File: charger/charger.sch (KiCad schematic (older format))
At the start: 1 part, among them U1 MSP432

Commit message: added aux power schem
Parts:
- added C1, C2: 1 uF, symbol Device:C_Small
- added C? (x2): 0.1 uF, symbol Device:C_Small
- added C?: 2.2 uF, symbol Device:CP
- added C?: 10 uF, symbol Device:CP
- added C?: 1 uF, symbol Device:CP
- added R?: 0 ohm, Resistor_SMD:R_1206_3216Metric, symbol Device:R_Small_US
- added R?: 0 ohm, symbol Device:R_Small_US
- added U2: NCP718xSN500, Package_TO_SOT_SMD:SOT-23-5, symbol Regulator_Linear:NCP718xSN500
- added U?: LF90_TO252, Package_TO_SOT_SMD:TO-252-2, symbol Regulator_Linear:LF90_TO252
- added U?: AP131-33, Package_TO_SOT_SMD:SOT-23-5, symbol Regulator_Linear:AP131-33
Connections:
- net labels added: +12V, +3.3V, +5V, +9V, GND
- wire segments 0 -> 60

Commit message: add power circuit
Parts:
- removed C?: 0.1 uF, symbol Device:C_Small
- removed C?: 2.2 uF, symbol Device:CP
- removed U?: LF90_TO252, Package_TO_SOT_SMD:TO-252-2, symbol Regulator_Linear:LF90_TO252
- added C?: 1000 uF, symbol Device:CP
- added C? (x3): 10 uF, symbol Device:C
- added C? (x2): 1000 pF, symbol Device:C
- added C? (x4): 1 uF, symbol Device:C
- added C?: 22 nF, symbol Device:C
- added C? (x2): 220 uF, symbol Device:C
- added C? (x2): 560 uF, symbol Device:C
- added C? (x2): 0.1 uF, symbol Device:C
- added D?: B1100B, symbol Device:D_Schottky
- added D? (x2): MUHA11013G, symbol Device:D
- added D? (x2): B1100-13, symbol Device:D_Schottky
- added L? (x2): 7443642200, symbol Device:L
- added L?: 220 uH, symbol Device:L
- added Q? (x4): CSD19531Q5A, Package_TO_SOT_SMD:TDSON-8-1, symbol Transistor_FET:CSD19531Q5A
- added R? (x2): 5.6 ohm, symbol Device:R_Small_US
- added R?: 430k, symbol Device:R_Small_US
- added R?: 169k, symbol Device:R_Small_US
- added R?: 3k, symbol Device:R_Small_US
- added R?: 3, symbol Device:R_Small_US
- added R?: 1k, symbol Device:R_Small_US
- added R? (x4): 2.21, symbol Device:R_Small_US
- added R? (x2): 4.42, symbol Device:R_Small_US
- added U?: LM5009MM, Package_SO:MSOP-8_3x3mm_P0.65mm, symbol Regulator_Switching:LM5009MM
- added U? (x2): LM5109BMA, Package_SO:SOIC-8_3.9x4.9mm_P1.27mm, symbol Driver_FET:LM5109BMA
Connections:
- net labels added: +10V, PWM_H1, PWM_H2, PWM_L1, PWM_L2, V_in, V_out, V_p
- net labels removed: +12V, +9V
- wire segments 60 -> 163

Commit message: added connectors
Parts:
- added J?: OSTT7020150, symbol Connector:Screw_Terminal_01x06
- added J?: OSTT7020150, symbol Connector:Screw_Terminal_01x02
- added TP? (x7): TestPoint, symbol Connector:TestPoint
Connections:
- net +10V: now also TP?.1
- net +3V3: now also TP?.1
- net +5V: now also TP?.1
- net at R?.2, U?.5 (LO): now also TP?.1 (x2)
- net at R?.2, U?.7 (HO): now also TP?.1 (x2)
- new net +BATT: J?.1 (Pin_1)
- new net -BATT: J?.2 (Pin_2)
- new net SP1+: J?.1 (Pin_1)
- new net SP1-: J?.2 (Pin_2), J?.3 (Pin_3)
- new net SP2-: J?.4 (Pin_4), J?.5 (Pin_5)
- new net SP3-: J?.6 (Pin_6)
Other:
- note added: "Based on TIDA-010042"
- note added: "Mark Ditsworth"
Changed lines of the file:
@@
 	9450 2550 9450 2650
 Wire Wire Line
-	10650 2250 10650 2550
+	10650 2250 10650 2400
 Connection ~ 10650 2550
 Wire Wire Line
@@
 Text Label 3650 3250 0    50   ~ 0
 PWM_L2
+$Comp
+L Connector:Screw_Terminal_01x06 J?
+U 1 1 5F1BBACF
+P 600 7350
+F 0 "J?" H 518 6917 50  0000 C CNN
+F 1 "OSTT7020150" H 680 7251 50  0001 L CNN
+F 2 "" H 600 7350 50  0001 C CNN
+F 3 "~" H 600 7350 50  0001 C CNN
+	1    600  7350
+	-1   0    0    1
+$EndComp
+$Comp
+L Connector:Screw_Terminal_01x02 J?
+U 1 1 5F1C245D
+P 6650 7400
+F 0 "J?" H 6730 7346 50  0000 L CNN
+F 1 "OSTT7020150" H 6730 7301 50  0001 L CNN
+F 2 "" H 6650 7400 50  0001 C CNN
+F 3 "~" H 6650 7400 50  0001 C CNN
+	1    6650 7400
+	1    0    0    -1
+$EndComp
+$Comp
+L Connector:TestPoint TP?
+U 1 1 5F1C5256
+P 9500 1050
+F 0 "TP?" V 9695 1122 50  0000 C CNN
+F 1 "TestPoint" V 9604 1122 50  0000 C CNN
+F 2 "" H 9700 1050 50  0001 C CNN
+F 3 "~" H 9700 1050 50  0001 C CNN
+	1    9500 1050
+	0    -1   -1   0
+$EndComp
+$Comp
+L Connector:TestPoint TP?
+U 1 1 5F1DAE48
+P 10750 1050
+F 0 "TP?" V 10704 1238 50  0000 L CNN
+F 1 "TestPoint" V 10795 1238 50  0000 L CNN
+F 2 "" H 10950 1050 50  0001 C CNN
+F 3 "~" H 10950 1050 50  0001 C CNN
+	1    10750 1050
+	0    1    1    0
+$EndComp
+$Comp
+L Connector:TestPoint TP?
+U 1 1 5F1DBECE
+P 10650 2400
+F 0 "TP?" V 10604 2588 50  0000 L CNN
+F 1 "TestPoint" V 10695 2588 50  0000 L CNN
+F 2 "" H 10850 2400 50  0001 C CNN
+F 3 "~" H 10850 2400 50  0001 C CNN
+	1    10650 2400
+	0    1    1    0
+$EndComp
+Connection ~ 10650 2400
+Wire Wire Line
+	10650 2400 10650 2550
+$Comp
+L Connector:TestPoint TP?
+U 1 1 5F1E3B56
+P 4950 2500
+F 0 "TP?" H 5008 2618 50  0000 L CNN
+F 1 "TestPoint" H 5008 2527 50  0000 L CNN
+F 2 "" H 5150 2500 50  0001 C CNN
+F 3 "~" H 5150 2500 50  0001 C CNN
+	1    4950 2500
+	1    0    0    -1
+$EndComp
+Connection ~ 4950 2500
+$Comp
+L Connector:TestPoint TP?
+U 1 1 5F1E6782
+P 5250 3350
+F 0 "TP?" V 5204 3538 50  0000 L CNN
+F 1 "TestPoint" V 5295 3538 50  0000 L CNN
+F 2 "" H 5450 3350 50  0001 C CNN
+F 3 "~" H 5450 3350 50  0001 C CNN
+	1    5250 3350
+	0    1    1    0
+$EndComp
+Connection ~ 5250 3350
+$Comp
+L Connector:TestPoint TP?
+U 1 1 5F1E781A
+P 5250 1750
+F 0 "TP?" V 5204 1938 50  0000 L CNN
+F 1 "TestPoint" V 5295 1938 50  0000 L CNN
+F 2 "" H 5450 1750 50  0001 C CNN
+F 3 "~" H 5450 1750 50  0001 C CNN
+	1    5250 1750
+	0    1    1    0
+$EndComp
+Connection ~ 5250 1750
+$Comp
+L Connector:TestPoint TP?
+U 1 1 5F1EFFDD
+P 4950 1000
+F 0 "TP?" H 5008 1118 50  0000 L CNN
+F 1 "TestPoint" H 5008 1027 50  0000 L CNN
+F 2 "" H 5150 1000 50  0001 C CNN
+F 3 "~" H 5150 1000 50  0001 C CNN
+	1    4950 1000
+	1    0    0    -1
+$EndComp
+Connection ~ 4950 1000
+Text Label 800  7550 0    50   ~ 0
+SP1+
+Text Label 800  7450 0    50   ~ 0
+SP1-
+Text Label 800  7350 0    50   ~ 0
+SP2+
+Text Label 800  7250 0    50   ~ 0
+SP2-
+Text Label 800  7150 0    50   ~ 0
+SP3+
+Text Label 800  7050 0    50   ~ 0
+SP3-
+Wire Wire Line
+	800  7350 800  7450
+Wire Wire Line
+	800  7150 800  7250
+$Comp
+L power:+BATT #PWR?
+U 1 1 5F24AB5C
+P 6450 7400
+F 0 "#PWR?" H 6450 7250 50  0001 C CNN
+F 1 "+BATT" H 6465 7573 50  0000 C CNN
+F 2 "" H 6450 7400 50  0001 C CNN
+F 3 "" H 6450 7400 50  0001 C CNN
+	1    6450 7400
+	1    0    0    -1
+$EndComp
+$Comp
+L power:-BATT #PWR?
+U 1 1 5F24D3B8
+P 6450 7500
+F 0 "#PWR?" H 6450 7350 50  0001 C CNN
+F 1 "-BATT" H 6465 7673 50  0000 C CNN
+F 2 "" H 6450 7500 50  0001 C CNN
+F 3 "" H 6450 7500 50  0001 C CNN
+	1    6450 7500
+	-1   0    0    1
+$EndComp
+Text Notes 10150 7350 0    89   ~ 0
+Mark Ditsworth
+Text Notes 7400 7500 0    89   ~ 0
+Based on TIDA-010042
 $EndSCHEMATC

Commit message: add ckt enable/disable
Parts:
- added C? (x2): 1200 uF, symbol Device:CP
- added C? (x5): 4.7 uF, symbol Device:C
- added C?: 0.1 uF, symbol Device:C
- added D?: D_Zener, symbol Device:D_Zener
- added Q? (x2): CSD18540Q5B, Package_TO_SOT_SMD:TDSON-8-1, symbol Transistor_FET:CSD18540Q5B
- added R? (x2): 0.002, symbol Device:R_US
- added R?: 5.11, symbol Device:R_US
- added R?: 10k, symbol Device:R_US
- added U?: UCC27517DBVR, symbol MSP_mwd:Generic_SOT23-5
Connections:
- net +10V: now also C?.2, U?.1
- net GND: now also C?.1, C?.2, C?.2, C?.2, C?.2, C?.2, C?.2, C?.2, D?.2 (A), Q?.1 (S), Q?.1 (S), Q?.2 (S), Q?.2 (S), Q?.3 (S), Q?.3 (S), U?.2, U?.4
- net SP1+: now also R?.2
- net SP3-: now also Q?.5 (D)
- net V_in: now also C?.1, C?.1, C?.1, C?.1, C?.1, C?.1, C?.1, R?.1
- net V_out: now also R?.1, R?.2
- net +BATT renamed +Bat
- net +Bat: now also R?.1
- net -BATT renamed -Bat
- net -Bat: now also Q?.5 (D)
- new net: Q?.4 (G), R?.1
- new net: R?.2, U?.5
- new net: D?.1 (K), Q?.4 (G), R?.2
- new net Input_EN: U?.3
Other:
- moved on the sheet: J?, U1

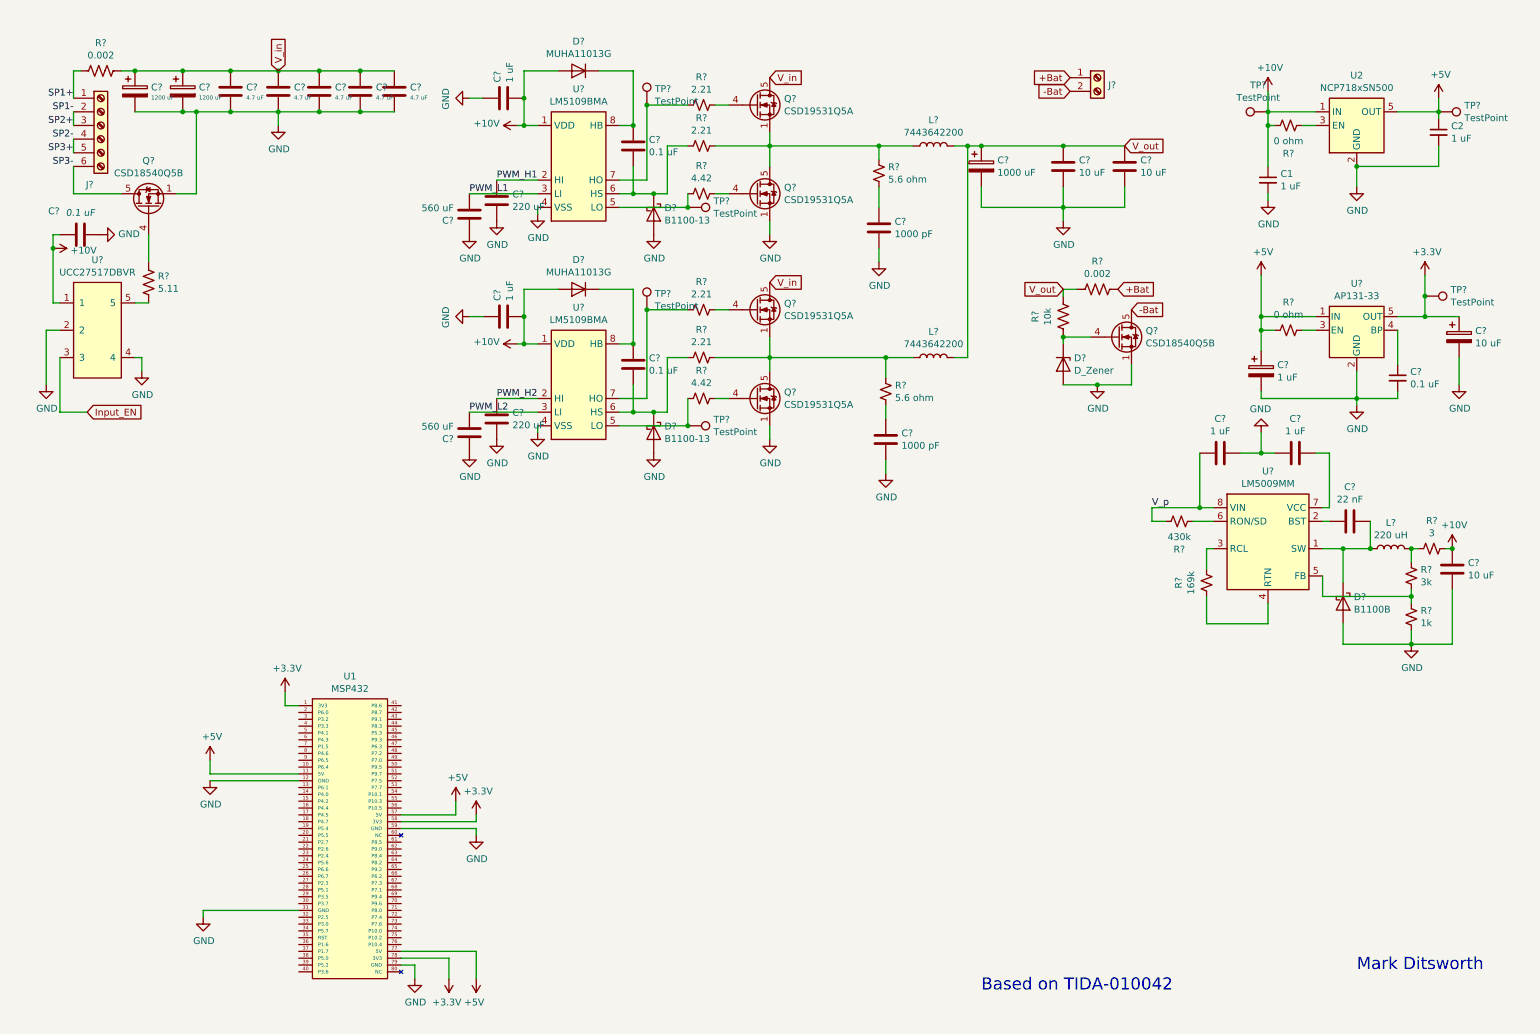
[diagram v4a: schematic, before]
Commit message: add voltage dividers
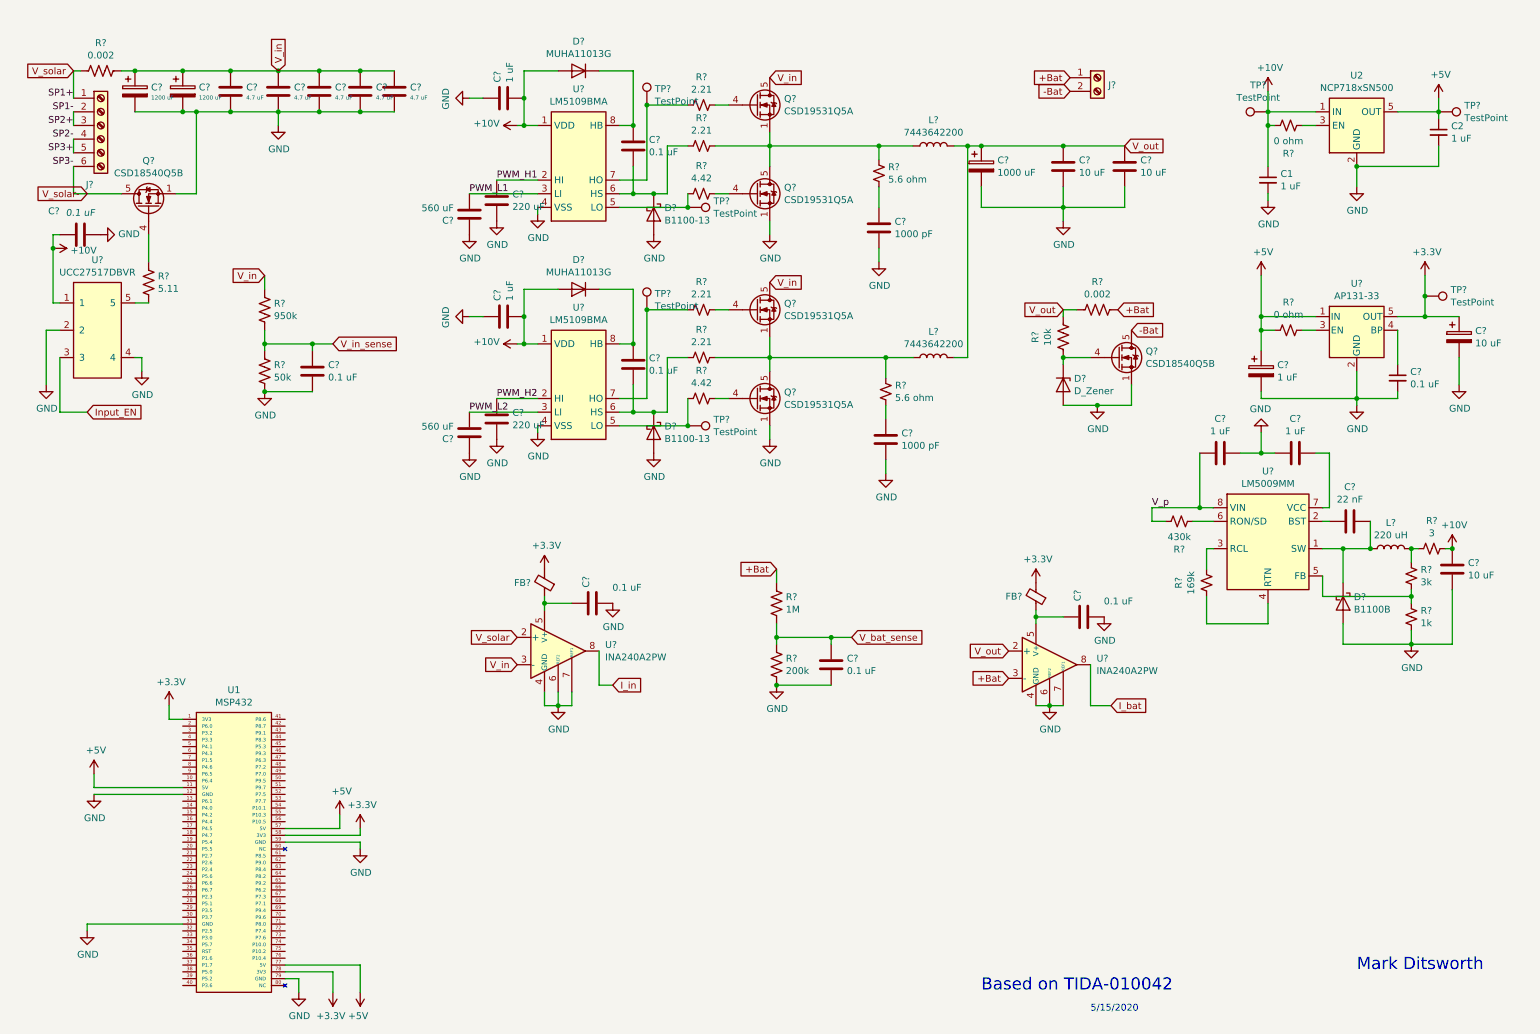
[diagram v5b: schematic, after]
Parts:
- added C? (x4): 0.1 uF, symbol Device:C
- added FB? (x2): 74279201, symbol Device:Ferrite_Bead_Small
- added R?: 950k, symbol Device:R_US
- added R?: 50k, symbol Device:R_US
- added R?: 1M, symbol Device:R_US
- added R?: 200k, symbol Device:R_US
- added U? (x2): INA240A2PW, Package_SO:TSSOP-8_4.4x3mm_P0.65mm, symbol Amplifier_Current:INA240A2PW
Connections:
- net +3V3: now also FB?.2, FB?.2
- net +Bat: now also R?.1, U?.3 (-)
- net GND: now also C?.2, C?.2, C?.2, C?.2, R?.2, R?.2, U?.1 (GND), U?.1 (GND), U?.4 (GND), U?.4 (GND), U?.6 (REF2), U?.6 (REF2), U?.7 (REF1), U?.7 (REF1)
- net V_in: now also R?.1, U?.3 (-)
- net V_out: now also U?.2 (+)
- net SP1+ renamed V_solar
- net V_solar: now also U?.2 (+)
- net SP3- renamed V_solar-
- new net: C?.1, FB?.1, U?.5 (V+) (x2)
- new net I_bat: U?.8
- new net I_in: U?.8
- new net V_bat_sense: C?.1, R?.1, R?.2
- new net V_in_sense: C?.1, R?.1, R?.2
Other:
- note added: "5/15/2020"
- moved on the sheet: D?, Q?, R?, U1

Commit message: begin with footprints
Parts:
- R? (x22): footprint (none) -> Resistor_SMD:R_1206_3216Metric
- U1: footprint (none) -> MWD_Footprints:MSP432
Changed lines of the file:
@@
 F 0 "U1" H 1925 5615 50  0000 C CNN
 F 1 "MSP432" H 1925 5524 50  0000 C CNN
-F 2 "" H 1650 5450 50  0001 C CNN
+F 2 "MWD_Footprints:MSP432" H 1650 5450 50  0001 C CNN
 F 3 "" H 1650 5450 50  0001 C CNN
 	1    1650 5450
@@
 F 0 "R?" V 9855 2650 50  0000 C CNN
 F 1 "0 ohm" V 9764 2650 50  0000 C CNN
-F 2 "" H 9650 2650 50  0001 C CNN
+F 2 "Resistor_SMD:R_1206_3216Metric" H 9650 2650 50  0001 C CNN
 F 3 "~" H 9650 2650 50  0001 C CNN
 	1    9650 2650
@@
 F 0 "R?" V 9055 4050 50  0000 C CNN
 F 1 "430k" V 8964 4050 50  0000 C CNN
-F 2 "" H 8850 4050 50  0001 C CNN
+F 2 "Resistor_SMD:R_1206_3216Metric" H 8850 4050 50  0001 C CNN
 F 3 "~" H 8850 4050 50  0001 C CNN
 	1    8850 4050
@@
 F 0 "R?" V 9255 4500 50  0000 C CNN
 F 1 "169k" V 9164 4500 50  0000 C CNN
-F 2 "" H 9050 4500 50  0001 C CNN
+F 2 "Resistor_SMD:R_1206_3216Metric" H 9050 4500 50  0001 C CNN
 F 3 "~" H 9050 4500 50  0001 C CNN
 	1    9050 4500
@@
 F 0 "R?" H 10618 4496 50  0000 L CNN
 F 1 "3k" H 10618 4405 50  0000 L CNN
-F 2 "" H 10550 4450 50  0001 C CNN
-F 3 "~" H 10550 4450 50  0001 C CNN
+F 2 "Resistor_SMD:R_1206_3216Metric" H 10550 4450 50  0001 C CNN
+F 3 "~" H 10550 4450 50  0001 C CNB
 	1    10550 4450
 	1    0    0    -1
@@
 F 0 "R?" V 10495 4250 50  0000 C CNN
 F 1 "3" V 10586 4250 50  0000 C CNN
-F 2 "" H 10700 4250 50  0001 C CNN
+F 2 "Resistor_SMD:R_1206_3216Metric" H 10700 4250 50  0001 C CNN
 F 3 "~" H 10700 4250 50  0001 C CNN
 	1    10700 4250
@@
 F 0 "R?" H 10618 4796 50  0000 L CNN
 F 1 "1k" H 10618 4705 50  0000 L CNN
-F 2 "" H 10550 4750 50  0001 C CNN
+F 2 "Resistor_SMD:R_1206_3216Metric" H 10550 4750 50  0001 C CNN
 F 3 "~" H 10550 4750 50  0001 C CNN
 	1    10550 4750
@@
 F 0 "R?" V 5145 1300 50  0000 C CNN
 F 1 "2.21" V 5236 1300 50  0000 C CNN
-F 2 "" H 5350 1300 50  0001 C CNN
+F 2 "Resistor_SMD:R_1206_3216Metric" H 5350 1300 50  0001 C CNN
 F 3 "~" H 5350 1300 50  0001 C CNN
 	1    5350 1300
@@
 F 0 "R?" V 5145 2850 50  0000 C CNN
 F 1 "2.21" V 5236 2850 50  0000 C CNN
-F 2 "" H 5350 2850 50  0001 C CNN
+F 2 "Resistor_SMD:R_1206_3216Metric" H 5350 2850 50  0001 C CNN
 F 3 "~" H 5350 2850 50  0001 C CNN
 	1    5350 2850
@@
 F 0 "R?" V 5145 1000 50  0000 C CNN
 F 1 "2.21" V 5236 1000 50  0000 C CNN
-F 2 "" H 5350 1000 50  0001 C CNN
+F 2 "Resistor_SMD:R_1206_3216Metric" H 5350 1000 50  0001 C CNN
 F 3 "~" H 5350 1000 50  0001 C CNN
 	1    5350 1000
@@
 F 0 "R?" V 5145 1650 50  0000 C CNN
 F 1 "4.42" V 5236 1650 50  0000 C CNN
-F 2 "" H 5350 1650 50  0001 C CNN
+F 2 "Resistor_SMD:R_1206_3216Metric" H 5350 1650 50  0001 C CNN
 F 3 "~" H 5350 1650 50  0001 C CNN
 	1    5350 1650
@@
 F 0 "R?" V 5145 3150 50  0000 C CNN
 F 1 "4.42" V 5236 3150 50  0000 C CNN
-F 2 "" H 5350 3150 50  0001 C CNN
+F 2 "Resistor_SMD:R_1206_3216Metric" H 5350 3150 50  0001 C CNN
 F 3 "~" H 5350 3150 50  0001 C CNN
 	1    5350 3150
@@
 F 0 "R?" V 5145 2500 50  0000 C CNN
 F 1 "2.21" V 5236 2500 50  0000 C CNN
-F 2 "" H 5350 2500 50  0001 C CNN
+F 2 "Resistor_SMD:R_1206_3216Metric" H 5350 2500 50  0001 C CNN
 F 3 "~" H 5350 2500 50  0001 C CNN
 	1    5350 2500
@@
 F 0 "R?" H 6768 3146 50  0000 L CNN
 F 1 "5.6 ohm" H 6768 3055 50  0000 L CNN
-F 2 "" H 6700 3100 50  0001 C CNN
+F 2 "Resistor_SMD:R_1206_3216Metric" H 6700 3100 50  0001 C CNN
 F 3 "~" H 6700 3100 50  0001 C CNN
 	1    6700 3100
@@
 F 0 "R?" H 6718 1546 50  0000 L CNN
 F 1 "5.6 ohm" H 6718 1455 50  0000 L CNN
-F 2 "" H 6650 1500 50  0001 C CNN
+F 2 "Resistor_SMD:R_1206_3216Metric" H 6650 1500 50  0001 C CNN
 F 3 "~" H 6650 1500 50  0001 C CNN
 	1    6650 1500
@@
 F 0 "R?" V 745 750 50  0000 C CNN
 F 1 "0.002" V 836 750 50  0000 C CNN
-F 2 "" V 990 740 50  0001 C CNN
+F 2 "Resistor_SMD:R_1206_3216Metric" V 990 740 50  0001 C CNN
 F 3 "~" H 950 750 50  0001 C CNN
 	1    950  750
@@
 F 0 "R?" H 1368 2346 50  0000 L CNN
 F 1 "5.11" H 1368 2255 50  0000 L CNN
-F 2 "" V 1340 2290 50  0001 C CNN
+F 2 "Resistor_SMD:R_1206_3216Metric" V 1340 2290 50  0001 C CNN
 F 3 "~" H 1300 2300 50  0001 C CNN
 	1    1300 2300
@@
 F 0 "R?" V 8045 2500 50  0000 C CNN
 F 1 "0.002" V 8136 2500 50  0000 C CNN
-F 2 "" V 8290 2490 50  0001 C CNN
+F 2 "Resistor_SMD:R_1206_3216Metric" V 8290 2490 50  0001 C CNN
 F 3 "~" H 8250 2500 50  0001 C CNN
 	1    8250 2500
@@
 F 0 "R?" V 7795 2700 50  0000 C CNN
 F 1 "10k" V 7886 2700 50  0000 C CNN
-F 2 "" V 8040 2690 50  0001 C CNN
+F 2 "Resistor_SMD:R_1206_3216Metric" V 8040 2690 50  0001 C CNN
 F 3 "~" H 8000 2700 50  0001 C CNN
 	1    8000 2700
@@
 F 0 "R?" H 2218 2546 50  0000 L CNN
 F 1 "950k" H 2218 2455 50  0000 L CNN
-F 2 "" V 2190 2490 50  0001 C CNN
+F 2 "Resistor_SMD:R_1206_3216Metric" V 2190 2490 50  0001 C CNN
 F 3 "~" H 2150 2500 50  0001 C CNN
 	1    2150 2500
@@
 F 0 "R?" H 2218 2996 50  0000 L CNN
 F 1 "50k" H 2218 2905 50  0000 L CNN
-F 2 "" V 2190 2940 50  0001 C CNN
+F 2 "Resistor_SMD:R_1206_3216Metric" V 2190 2940 50  0001 C CNN
 F 3 "~" H 2150 2950 50  0001 C CNN
 	1    2150 2950
@@
 F 0 "R?" H 5968 4696 50  0000 L CNN
 F 1 "1M" H 5968 4605 50  0000 L CNN
-F 2 "" V 5940 4640 50  0001 C CNN
+F 2 "Resistor_SMD:R_1206_3216Metric" V 5940 4640 50  0001 C CNN
 F 3 "~" H 5900 4650 50  0001 C CNN
 	1    5900 4650
@@
 F 0 "R?" H 5968 5146 50  0000 L CNN
 F 1 "200k" H 5968 5055 50  0000 L CNN
-F 2 "" V 5940 5090 50  0001 C CNN
+F 2 "Resistor_SMD:R_1206_3216Metric" V 5940 5090 50  0001 C CNN
 F 3 "~" H 5900 5100 50  0001 C CNN
 	1    5900 5100
